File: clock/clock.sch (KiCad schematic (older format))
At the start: 169 parts, among them J1 Conn_01x06_Female, P1 Conn_WallPlug, T1 120 to 12, U1 NPIC6C596A, U10 NPIC6C596A, U11 PIC18F45K20_44-PIN_TQFP, U2 NPIC6C596A, U3 NPIC6C596A, U4 NPIC6C596A, U5 NPIC6C596A, U6 NPIC6C596A, U7 L78L33ABU, U8 NPIC6C596A, U9 NPIC6C596A

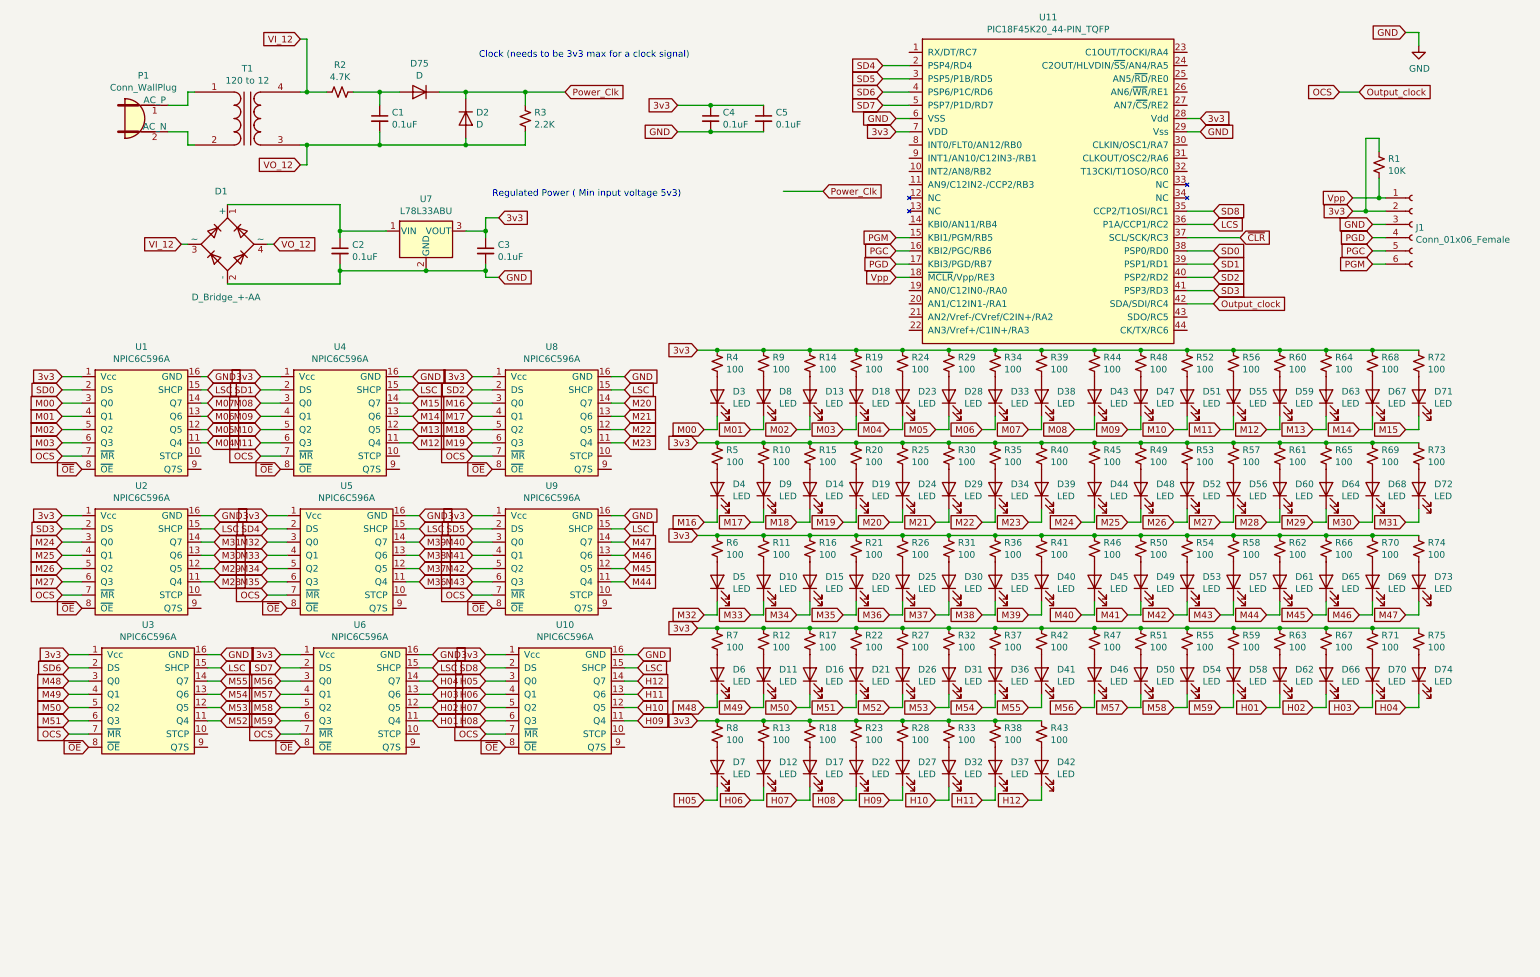
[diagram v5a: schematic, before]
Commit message: Reroute the shift registers
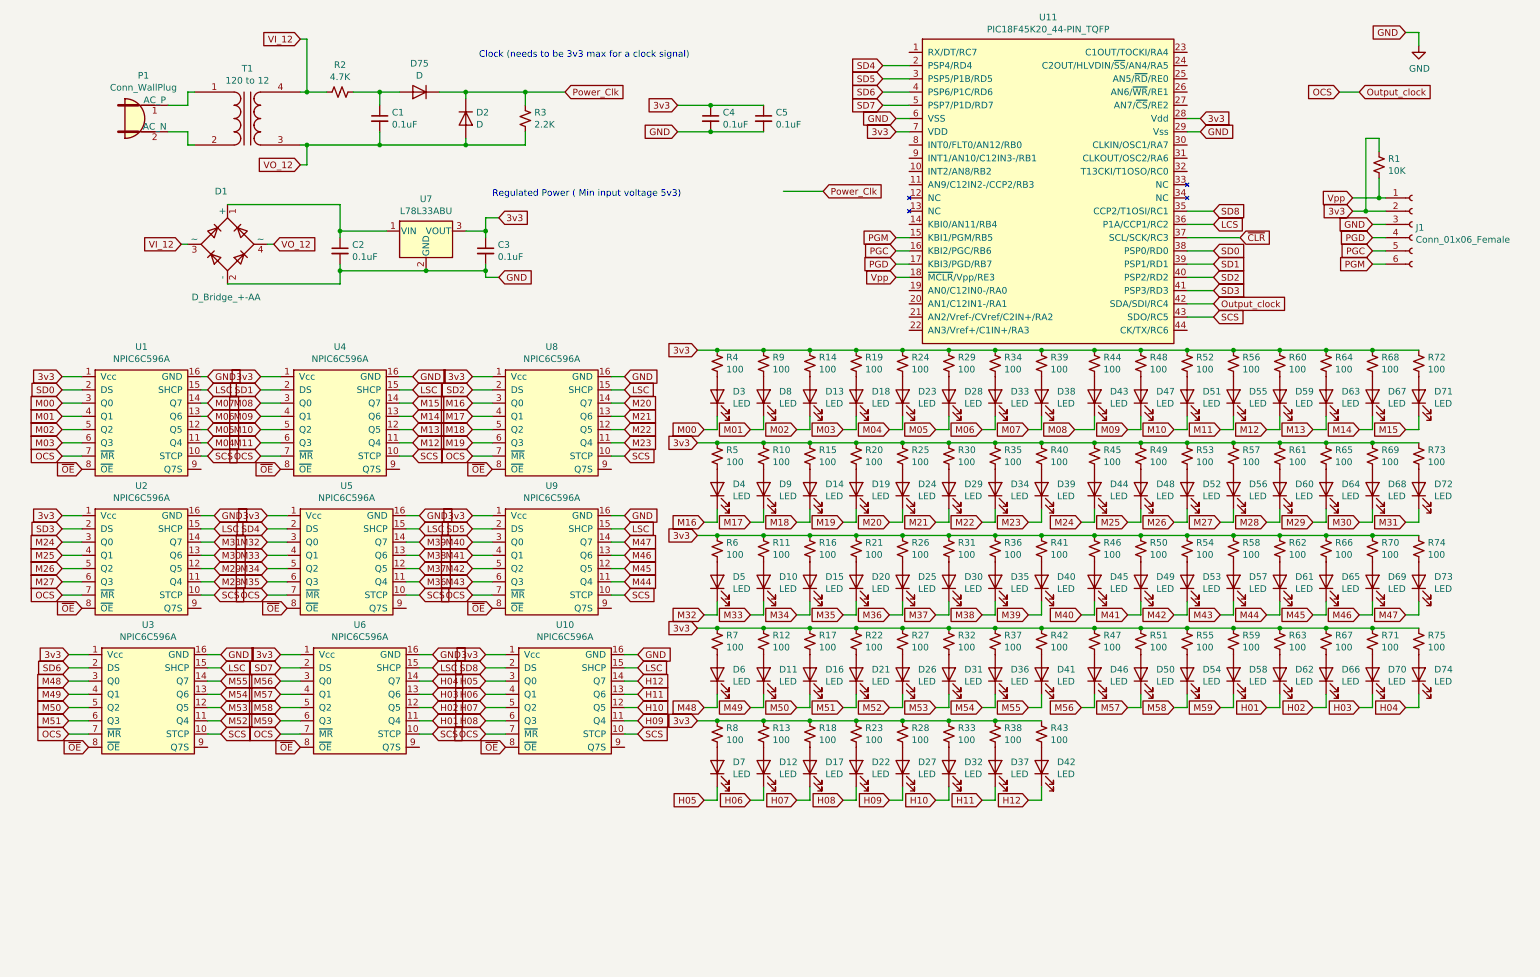
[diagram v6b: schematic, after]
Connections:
- net SCS: now reaches U11.43 (SDO/RC5)
- net SCS: now also U1.10 (STCP), U10.10 (STCP), U2.10 (STCP), U3.10 (STCP), U4.10 (STCP), U5.10 (STCP), U6.10 (STCP), U8.10 (STCP), U9.10 (STCP)
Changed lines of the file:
@@
 Wire Wire Line
 	3800 3200 3950 3200
+Text GLabel 9400 2750 2    50   Input ~ 0
+SCS
+Wire Wire Line
+	9400 2750 9200 2750
+Text GLabel 1800 3800 2    50   Input ~ 0
+SCS
+Wire Wire Line
+	1800 3800 1750 3800
+Text GLabel 3350 3800 2    50   Input ~ 0
+SCS
+Wire Wire Line
+	3350 3800 3250 3800
+Text GLabel 4950 3800 2    50   Input ~ 0
+SCS
+Wire Wire Line
+	4950 3800 4850 3800
+Text GLabel 4950 4850 2    50   Input ~ 0
+SCS
+Wire Wire Line
+	4950 4850 4850 4850
+Text GLabel 3400 4850 2    50   Input ~ 0
+SCS
+Wire Wire Line
+	3400 4850 3300 4850
+Text GLabel 1850 4850 2    50   Input ~ 0
+SCS
+Wire Wire Line
+	1850 4850 1750 4850
+Text GLabel 1900 5900 2    50   Input ~ 0
+SCS
+Wire Wire Line
+	1900 5900 1800 5900
+Text GLabel 3500 5900 2    50   Input ~ 0
+SCS
+Wire Wire Line
+	3500 5900 3400 5900
+Text GLabel 5050 5900 2    50   Input ~ 0
+SCS
+Wire Wire Line
+	5050 5900 4950 5900
 $EndSCHEMATC

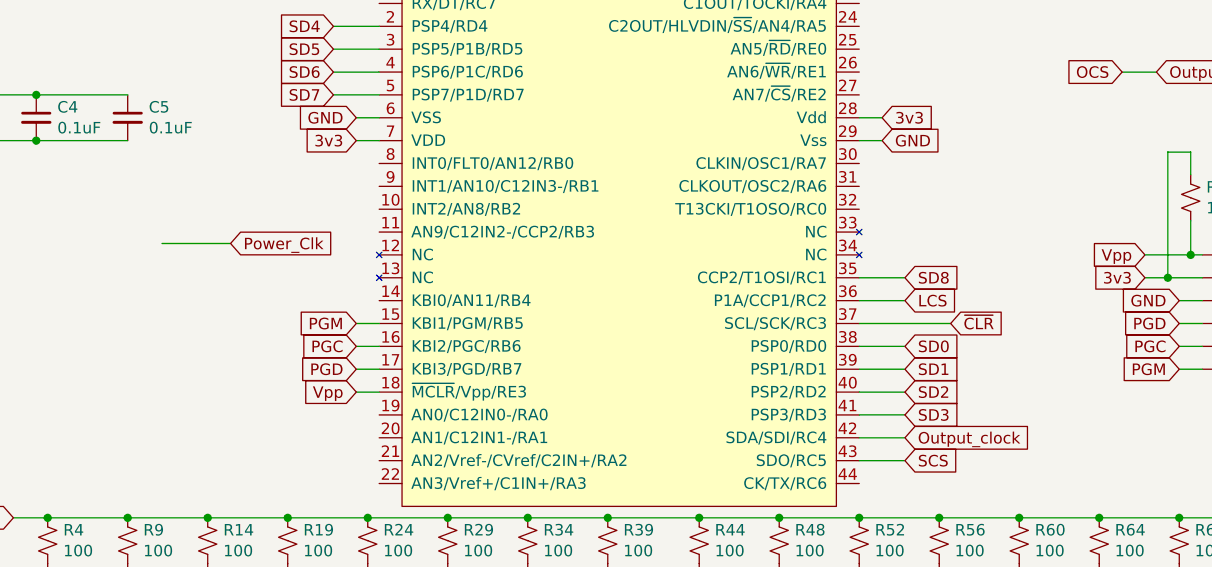
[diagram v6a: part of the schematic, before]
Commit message: Need to route power. Considering expanding the board.
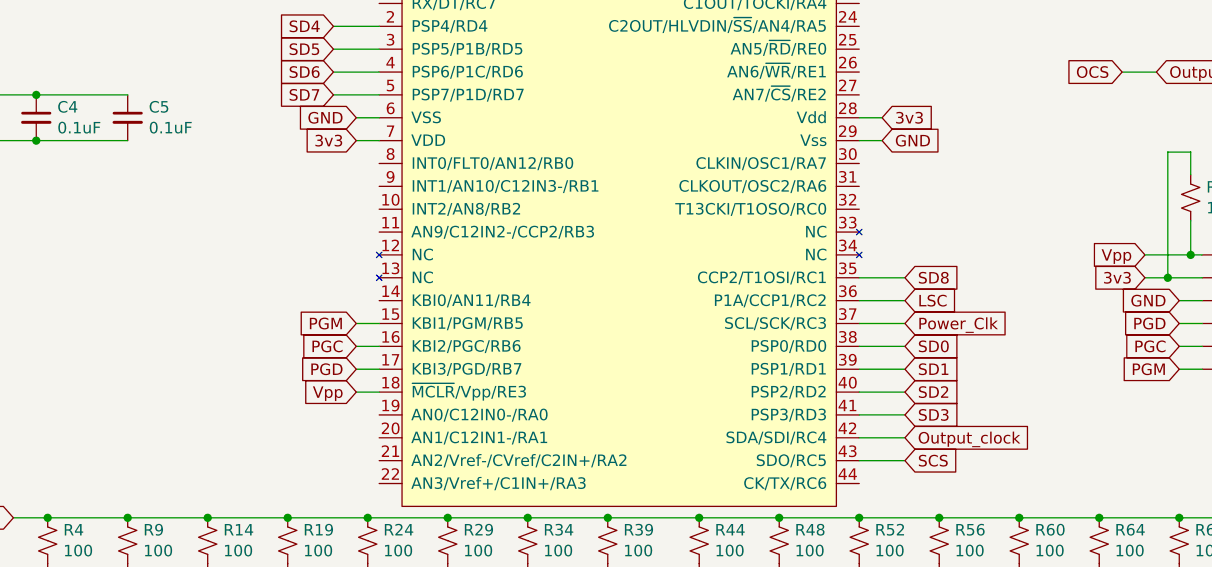
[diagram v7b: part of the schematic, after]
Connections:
- net LCS is gone; now on net LSC: U11.36 (P1A/CCP1/RC2)
- net ~CLR is gone; now on net Power_Clk: U11.37 (SCL/SCK/RC3)
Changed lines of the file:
@@
 $EndComp
 Text GLabel 9400 2050 2    50   Input ~ 0
-LCS
+LSC
 Wire Wire Line
 	9400 2050 9200 2050
@@
 Text GLabel 3900 5900 0    50   Input ~ 0
 OCS
-Text GLabel 9600 2150 2    50   Input ~ 0
-~CLR
-Wire Wire Line
-	9200 2150 9600 2150
+Wire Wire Line
+	9200 2150 9400 2150
 $Comp
 L MCU_PIC_18F:PIC18F45K20_44-PIN_TQFP U11
@@
 	4200 1050 4500 1050
 Connection ~ 4200 1050
-Text GLabel 6450 1800 2    50   Input ~ 0
+Text GLabel 9400 2150 2    50   Input ~ 0
 Power_Clk
-Wire Wire Line
-	6150 1800 6450 1800
 $Comp
 L Shift_reg:NPIC6C596A U1

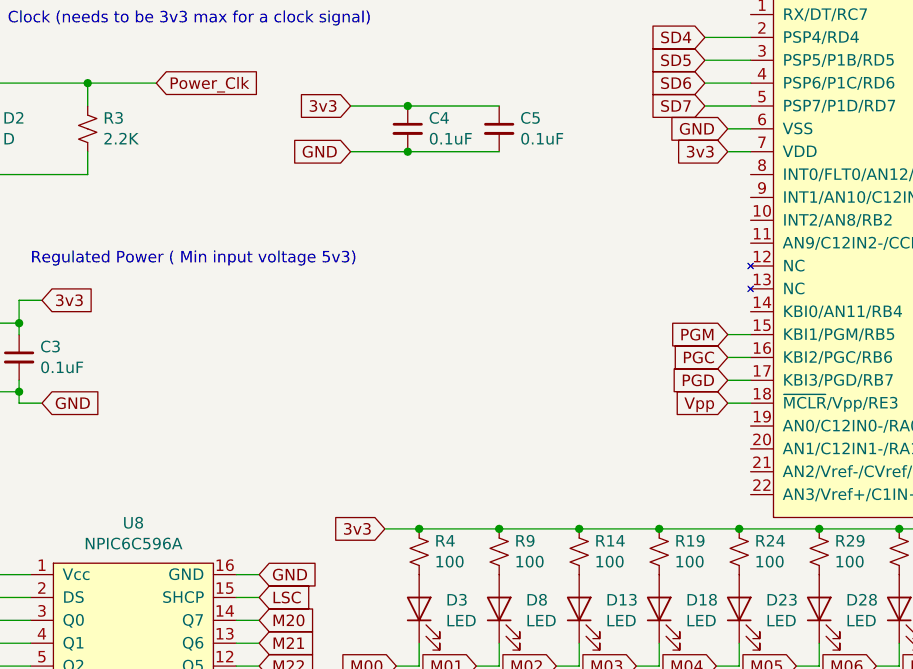
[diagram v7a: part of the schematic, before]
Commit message: TODO: Trace power domains.
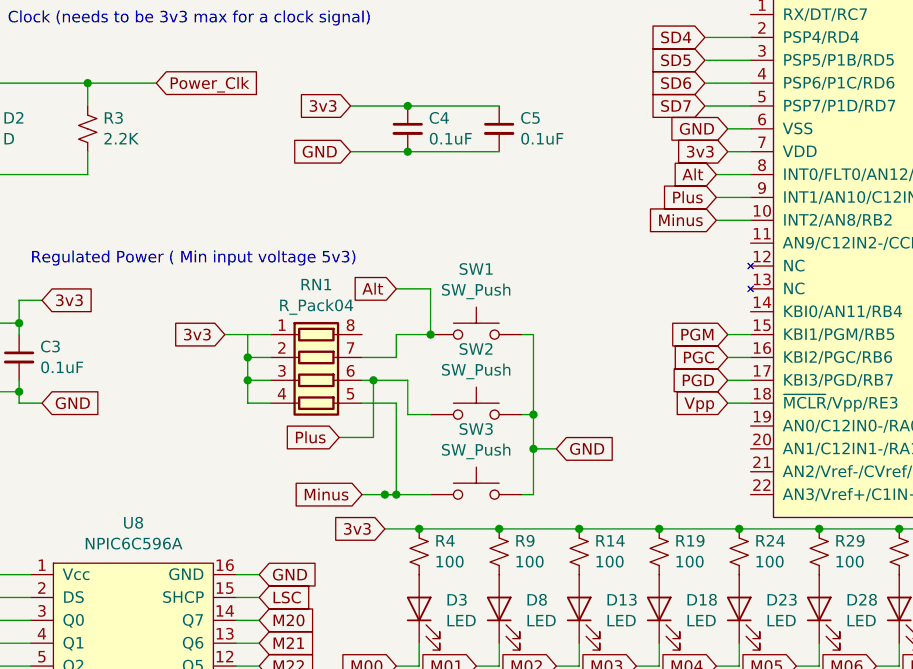
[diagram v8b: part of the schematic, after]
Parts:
- added RN1: R_Pack04, Resistor_SMD:R_Array_Concave_4x0603, symbol Device:R_Pack04
- added SW1, SW2, SW3: SW_Push, cap_touch_LPC804_NXP:LL3301FF065QJ, symbol Switch:SW_Push
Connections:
- net 3v3: now also RN1.1 (R1.1), RN1.2 (R2.1), RN1.3 (R3.1), RN1.4 (R4.1)
- net GND: now also SW1.2, SW2.2, SW3.2
- net Minus: now reaches U11.10 (INT2/AN8/RB2)
- net Minus: now also RN1.5 (R4.2), SW3.1
- net Alt: now reaches U11.8 (INT0/FLT0/AN12/RB0)
- net Alt: now also RN1.7 (R2.2), SW1.1
- net Plus: now reaches U11.9 (INT1/AN10/C12IN3-/RB1)
- net Plus: now also RN1.6 (R3.2), SW2.1
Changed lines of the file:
@@
 Wire Wire Line
 	5050 5900 4950 5900
+$Comp
+L Switch:SW_Push SW1
+U 1 1 5E2A23A0
+P 5900 2150
+F 0 "SW1" H 5900 2435 50  0000 C CNN
+F 1 "SW_Push" H 5900 2344 50  0000 C CNN
+F 2 "cap_touch_LPC804_NXP:LL3301FF065QJ" H 5900 2350 50  0001 C CNN
+F 3 "" H 5900 2350 50  0001 C CNN
+	1    5900 2150
+	1    0    0    -1
+$EndComp
+$Comp
+L Switch:SW_Push SW2
+U 1 1 5E2A2778
+P 5900 2500
+F 0 "SW2" H 5900 2785 50  0000 C CNN
+F 1 "SW_Push" H 5900 2694 50  0000 C CNN
+F 2 "cap_touch_LPC804_NXP:LL3301FF065QJ" H 5900 2700 50  0001 C CNN
+F 3 "" H 5900 2700 50  0001 C CNN
+	1    5900 2500
+	1    0    0    -1
+$EndComp
+$Comp
+L Switch:SW_Push SW3
+U 1 1 5E2E41F6
+P 5900 2850
+F 0 "SW3" H 5900 3135 50  0000 C CNN
+F 1 "SW_Push" H 5900 3044 50  0000 C CNN
+F 2 "cap_touch_LPC804_NXP:LL3301FF065QJ" H 5900 3050 50  0001 C CNN
+F 3 "" H 5900 3050 50  0001 C CNN
+	1    5900 2850
+	1    0    0    -1
+$EndComp
+$Comp
+L Device:R_Pack04 RN1
+U 1 1 5E326030
+P 5200 2350
+F 0 "RN1" V 4783 2350 50  0000 C CNN
+F 1 "R_Pack04" V 4874 2350 50  0000 C CNN
+F 2 "Resistor_SMD:R_Array_Concave_4x0603" V 5475 2350 50  0001 C CNN
+F 3 "~" H 5200 2350 50  0001 C CNN
+	1    5200 2350
+	0    1    1    0
+$EndComp
+Wire Wire Line
+	5400 2250 5550 2250
+Wire Wire Line
+	5550 2250 5550 2150
+Wire Wire Line
+	5550 2150 5700 2150
+Wire Wire Line
+	5600 2350 5600 2500
+Wire Wire Line
+	5600 2500 5700 2500
+Wire Wire Line
+	5400 2350 5450 2350
+Wire Wire Line
+	5550 2450 5550 2850
+Wire Wire Line
+	5550 2850 5700 2850
+Wire Wire Line
+	5400 2450 5550 2450
+Wire Wire Line
+	5000 2150 4900 2150
+Wire Wire Line
+	4900 2150 4900 2250
+Wire Wire Line
+	4900 2250 5000 2250
+Wire Wire Line
+	4900 2250 4900 2350
+Wire Wire Line
+	4900 2350 5000 2350
+Connection ~ 4900 2250
+Wire Wire Line
+	4900 2350 4900 2450
+Wire Wire Line
+	4900 2450 5000 2450
+Connection ~ 4900 2350
+Text GLabel 4800 2150 0    50   Input ~ 0
+3v3
+Wire Wire Line
+	4800 2150 4900 2150
+Text GLabel 6250 2650 2    50   Input ~ 0
+GND
+Wire Wire Line
+	6150 2650 6250 2650
+Wire Wire Line
+	6100 2150 6150 2150
+Wire Wire Line
+	6150 2150 6150 2500
+Wire Wire Line
+	6100 2500 6150 2500
+Connection ~ 6150 2500
+Wire Wire Line
+	6150 2500 6150 2650
+Wire Wire Line
+	6100 2850 6150 2850
+Wire Wire Line
+	6150 2850 6150 2650
+Connection ~ 6150 2650
+Text GLabel 6950 1450 0    50   Input ~ 0
+Alt
+Text GLabel 6950 1550 0    50   Input ~ 0
+Plus
+Text GLabel 6950 1650 0    50   Input ~ 0
+Minus
+Wire Wire Line
+	6950 1450 7100 1450
+Wire Wire Line
+	6950 1550 7100 1550
+Wire Wire Line
+	6950 1650 7100 1650
+Text GLabel 5550 1950 0    50   Input ~ 0
+Alt
+Wire Wire Line
+	5550 1950 5700 1950
+Wire Wire Line
+	5700 1950 5700 2150
+Connection ~ 5700 2150
+Text GLabel 5300 2600 0    50   Input ~ 0
+Plus
+Wire Wire Line
+	5300 2600 5450 2600
+Wire Wire Line
+	5450 2600 5450 2350
+Connection ~ 5450 2350
+Wire Wire Line
+	5450 2350 5600 2350
+Text GLabel 5400 2850 0    50   Input ~ 0
+Minus
+Wire Wire Line
+	5400 2850 5500 2850
+Wire Wire Line
+	5500 2850 5550 2850
+Connection ~ 5500 2850
+Wire Wire Line
+	5500 2850 5550 2850
+Connection ~ 5550 2850
 $EndSCHEMATC
